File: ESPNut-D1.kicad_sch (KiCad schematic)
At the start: 53 parts, among them J1 USB_C_Receptacle_USB2.0, J2 ESP_CONN, J3 USB_PADS, J4 ESP_PROG, Q1 BC817, Q2 BC817, Q3 Si2302CDS, SW1 ESP_RST, SW2 ESP_BOOT, SW3 ESP_VDD_SW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

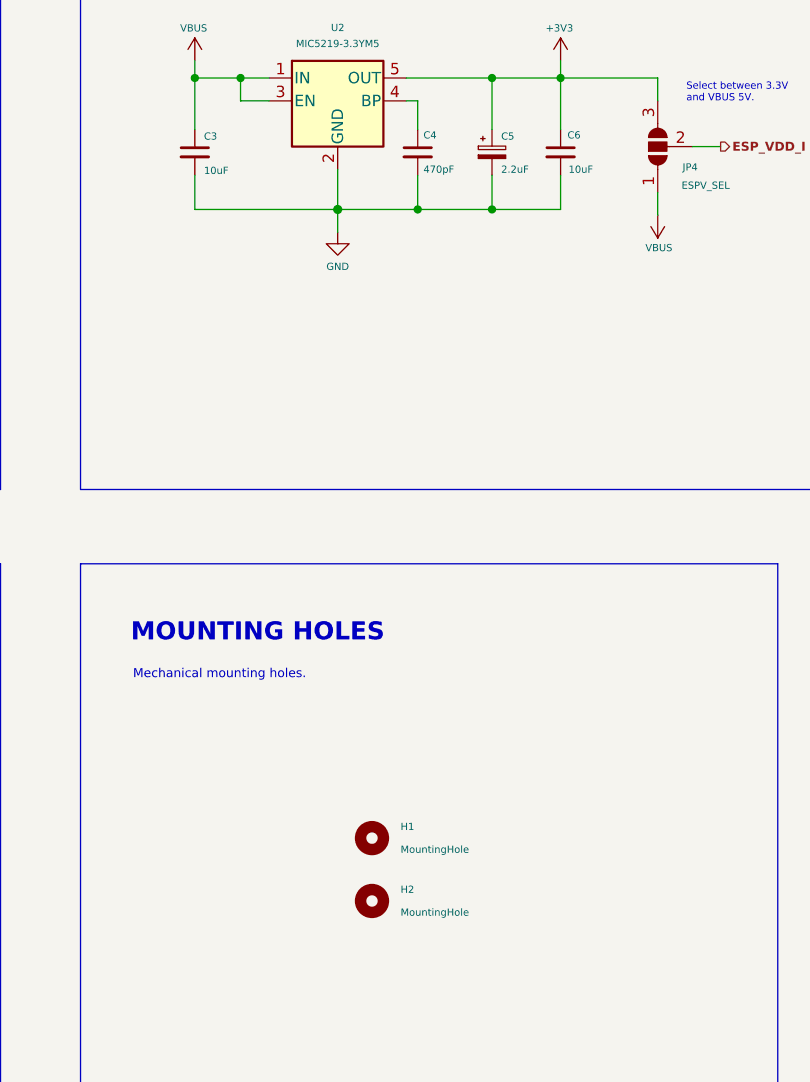
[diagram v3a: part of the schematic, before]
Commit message: Updated BoM
- Updated BoM.
  - Assigned all MPNs.
  - Changed the 10 uF, 0402 capacitor to 4.7 uF, 0402.
- Imported all changes to the PCB.
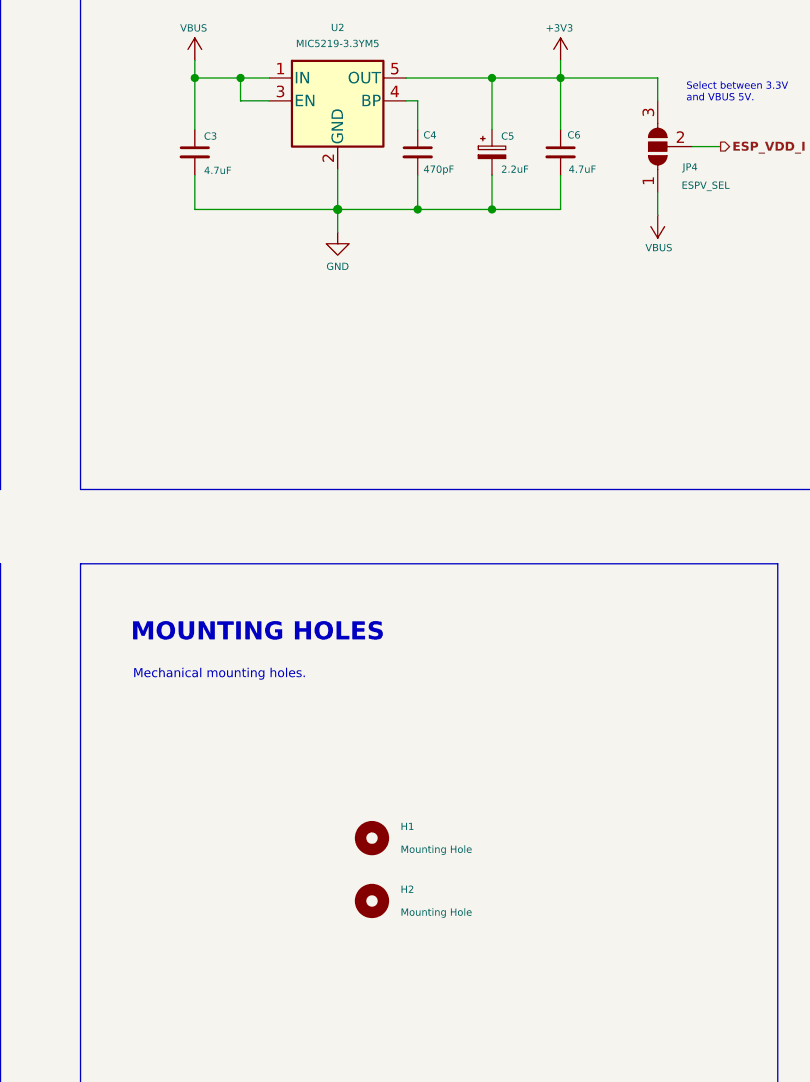
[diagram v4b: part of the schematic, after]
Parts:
- C1, C2: MFR (none) -> Yageo; MPN (none) -> CC0402KRX5R6BB104
- C3, C6: value 10uF -> 4.7uF; MFR (none) -> Yageo; MPN (none) -> CC0402MRX5R5BB475
- C4: MFR (none) -> Walsin; MPN (none) -> 0402N471J500LT
- C5: MFR (none) -> KYOCERA AVX; MPN (none) -> TAJR225M016RNJ
- D1, D4: MFR (none) -> Nexperia; MPN (none) -> RB751V40
- D2: MFR (none) -> Everlight; MPN (none) -> 19-21SURC/S530-A2/TR8
- D5: MFR (none) -> Everlight; MPN (none) -> 19-217UYOC/S3112/TR8
- H1, H2: value MountingHole -> Mounting Hole; MFR (none) -> DNP; MPN (none) -> DNP
- J1: MFR Korean Hroparts Elec -> Yi Yuan; MPN TYPE-C-31-M-12 -> YTC-TC16-273A1
- J2, J3, J4, JP1, JP2, JP3, JP4, JP5, JP6, TP1, TP10, TP11, TP2, TP3, TP4, TP5, TP6, TP7, TP8, TP9: MFR (none) -> DNP; MPN (none) -> DNP
- Q1, Q2: MFR (none) -> Nexperia; MPN (none) -> BC817-16,215
- Q3: MFR (none) -> Vishay; MPN (none) -> Si2302CDS
- R1, R5, R9: MFR (none) -> Yageo; MPN (none) -> RC0402FR-7D220RL
- R4, R7: MFR (none) -> Walsin; MPN (none) -> WR04X1002FTL
- SW1, SW2, SW4: MFR (none) -> USAKRO; MPN (none) -> UK-B0273-SP25Y
- SW3: MFR (none) -> C&K; MPN (none) -> PCM12SMTR
- U1: MFR (none) -> WCH; MPN (none) -> CH340G
- U2: MFR (none) -> Microchip; MPN (none) -> MIC5219-3.3YM5
- Y1: MFR (none) -> Murata; MPN (none) -> CSTNE12M0G52Z000R0

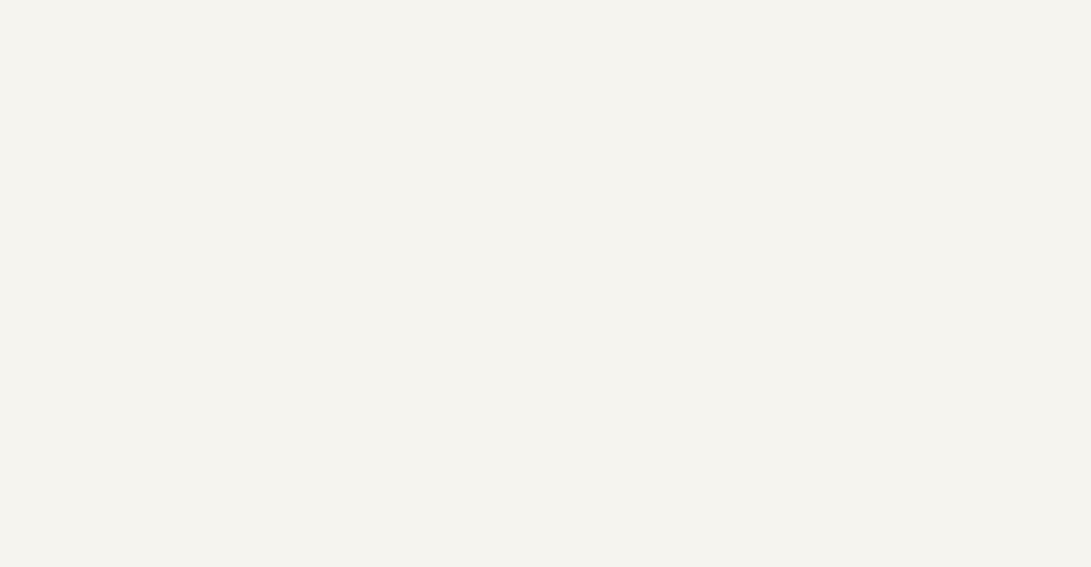
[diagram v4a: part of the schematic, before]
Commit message: Generated manufacturing files
- Added KiExport configuration and script.
- Added dimension drawings.
- Added board characteristics and stackup table.
- Added `OSHW` logo.
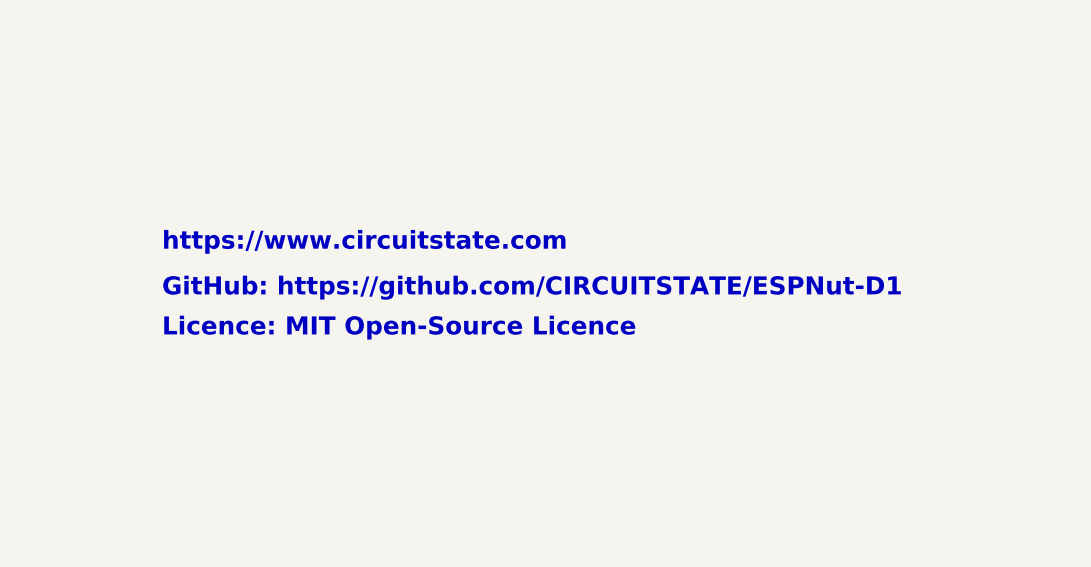
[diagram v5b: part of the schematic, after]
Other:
- note added: "GitHub: https://github.com/CIRCUITSTATE/ESPNut-D1"
- note added: "Licence: MIT Open-Source Licence"
- note added: "https://www.circuitstate.com"
- company: CIRCUITSTATE Electronics LLP -> CIRCUITSTATE Electronics LLP (www.circuitstate.com)
